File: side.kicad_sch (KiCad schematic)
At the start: 83 parts, among them J1 Conn_01x02, J2 SWD_Connector, J3 USB_C_Receptacle_USB2.0_14P, SW1 Reset Button, SW10 SW_Push, SW11 SW_Push, SW12 SW_Push, SW13 SW_Push, SW14 SW_Push, SW15 SW_Push, SW16 SW_Push, SW17 SW_Push, SW18 SW_Push, SW19 SW_Push, SW2 SW_On_Off, SW20 SW_Push, SW21 SW_Push, SW22 SW_Push, SW23 SW_Push, SW3 SW_Push, SW4 SW_Push, SW5 SW_Push, SW6 SW_Push, SW7 SW_Push, SW8 SW_Push, SW9 SW_Push, U1 nRF52840, U2 USBLC6-2SC6, Y1 JYJE 2TJ432000NYFBC

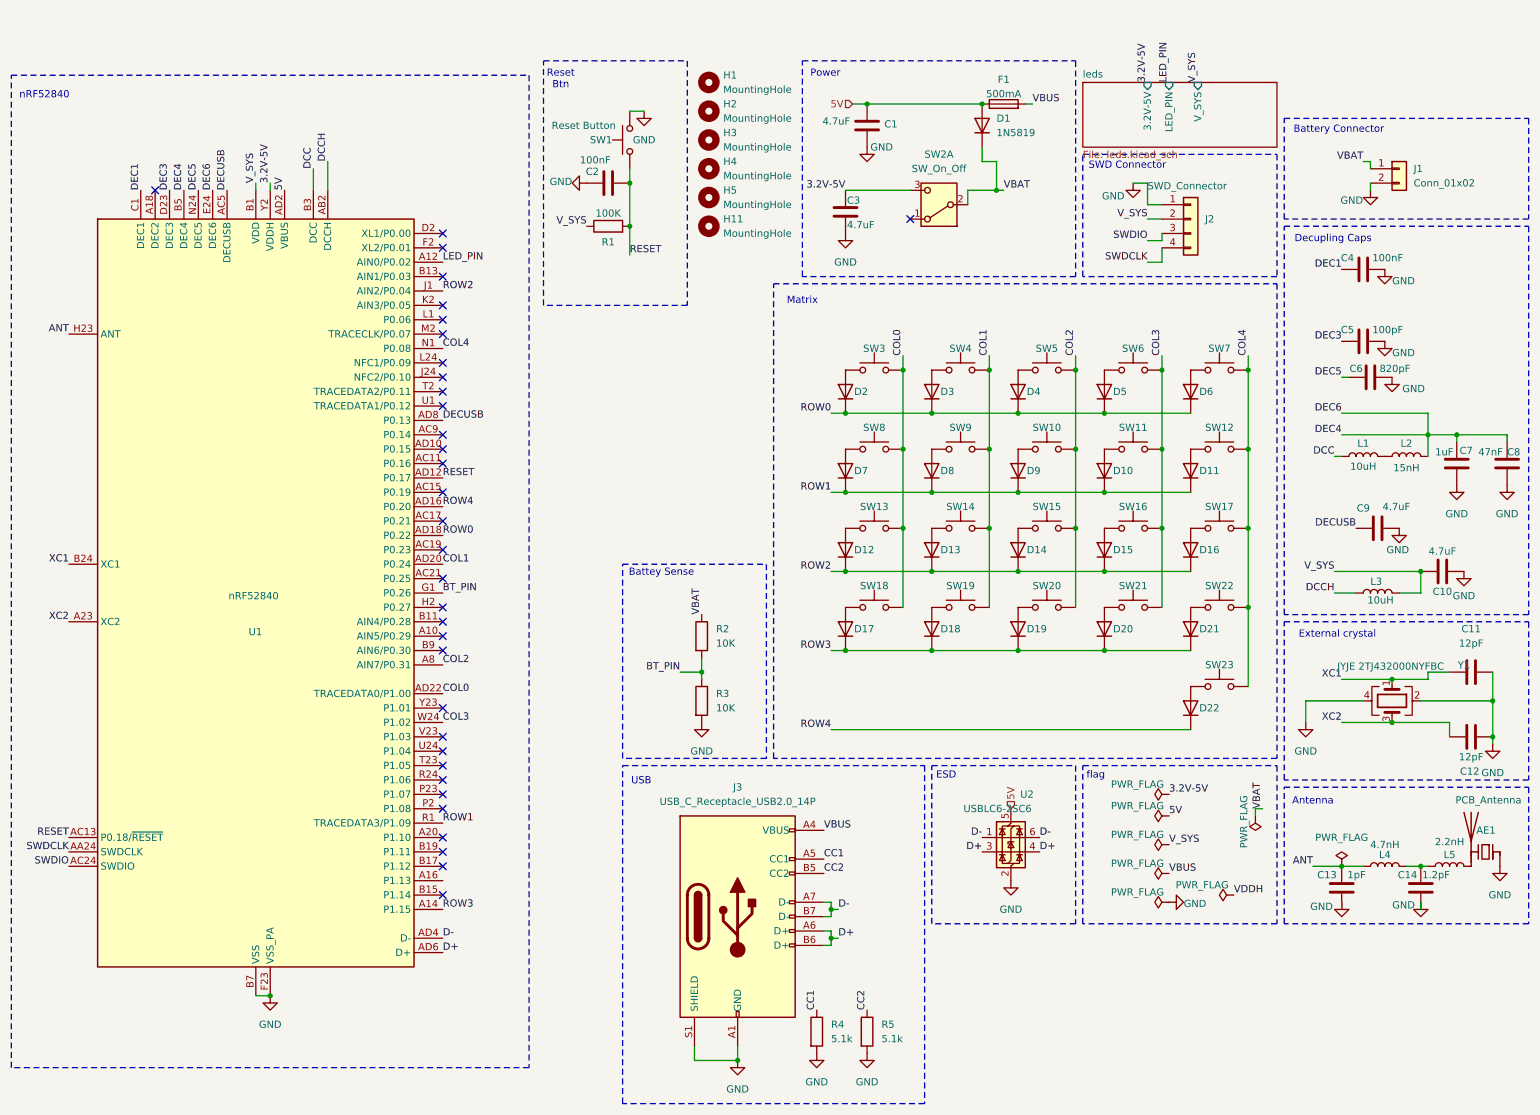
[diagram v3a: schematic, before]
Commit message: wired up the new votlage converter, removed small smd componenets
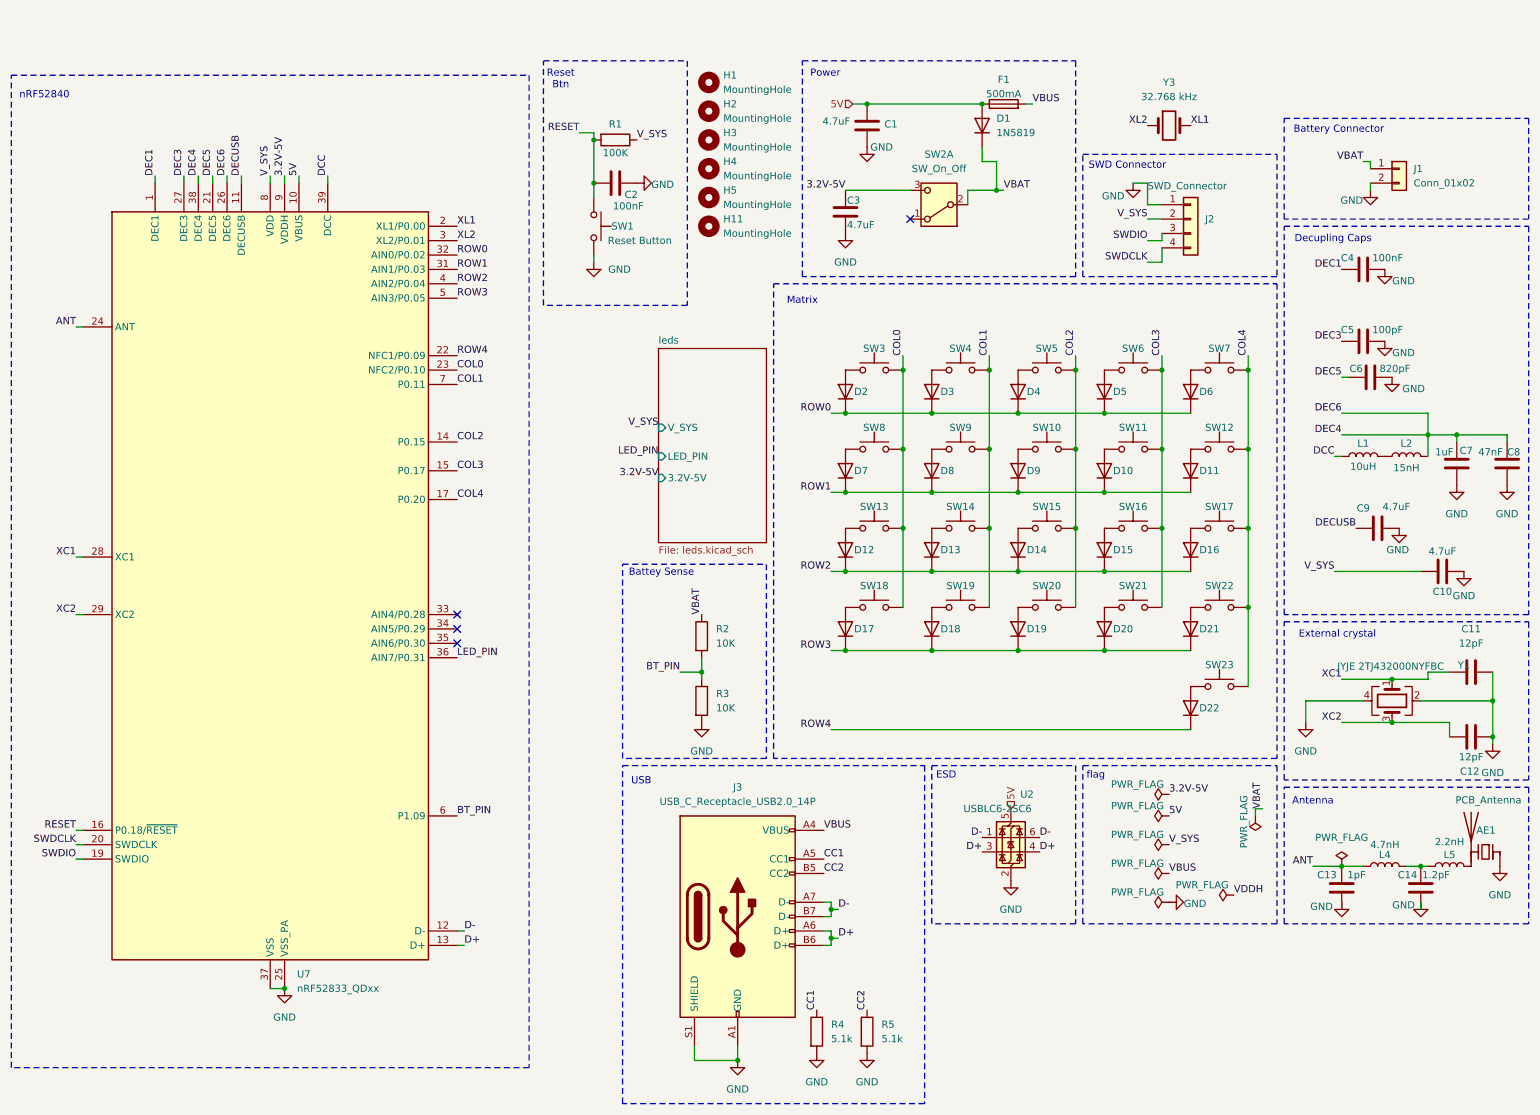
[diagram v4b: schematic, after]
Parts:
- removed L3: 10uH, Inductor_SMD:L_1008_2520Metric, symbol Device:L
- removed U1: nRF52840, Package_DFN_QFN:Nordic_AQFN-73-1EP_7x7mm_P0.5mm, symbol MCU_Nordic:nRF52840
- added U7: nRF52833_QDxx, Package_DFN_QFN:QFN-40-1EP_5x5mm_P0.4mm_EP3.6x3.6mm, symbol MCU_Nordic:nRF52833_QDxx
- added Y3: 32.768 kHz, Crystal:Crystal_SMD_3215-2Pin_3.2x1.5mm, symbol Device:Crystal
- C1, C10, C11, C12, C13, C14, C2, C3, C4, C5, C6, C7, C8, C9: footprint Capacitor_SMD:C_0402_1005Metric -> Capacitor_SMD:C_0603_1608Metric
- R1, R2, R3, R4, R5: footprint Resistor_SMD:R_0201_0603Metric -> Resistor_SMD:R_0402_1005Metric
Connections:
- net 3.2V-5V: now also U7.9 (VDDH)
- net 5V: now also U7.10 (VBUS)
- net ANT: now also U7.24 (ANT)
- net BT_PIN: now also U7.6 (P1.09)
- net COL0: now also U7.23 (NFC2/P0.10)
- net COL1: now also U7.7 (P0.11)
- net COL2: now also U7.14 (P0.15)
- net COL3: now also U7.15 (P0.17)
- net COL4: now also U7.17 (P0.20)
- net D+: now also U7.13 (D+)
- net D-: now also U7.12 (D-)
- net DCC: now also U7.39 (DCC)
- net DEC1: now also U7.1 (DEC1)
- net DEC3: now also U7.27 (DEC3)
- net DEC4: now also U7.26 (DEC6), U7.38 (DEC4)
- net DEC5: now also U7.21 (DEC5)
- net DECUSB: now also U7.11 (DECUSB)
- net GND: now also U7.25 (VSS_PA), U7.37 (VSS), U7.41 (VSS)
- net LED_PIN: now also U7.36 (AIN7/P0.31)
- net RESET: now also U7.16 (P0.18/~{RESET})
- net ROW0: now also U7.32 (AIN0/P0.02)
- net ROW1: now also U7.31 (AIN1/P0.03)
- net ROW2: now also U7.4 (AIN2/P0.04)
- net ROW3: now also U7.5 (AIN3/P0.05)
- net ROW4: now also U7.22 (NFC1/P0.09)
- net SWDCLK: now also U7.20 (SWDCLK)
- net SWDIO: now also U7.19 (SWDIO)
- net V_SYS: now also U7.18 (VDD), U7.30 (VDD), U7.40 (VDD), U7.8 (VDD)
- net XC1: now also U7.28 (XC1)
- net XC2: now also U7.29 (XC2)
- new net XL1: U7.2 (XL1/P0.00), Y3.2
- new net XL2: U7.3 (XL2/P0.01), Y3.1
- no-connect marks 34 -> 4
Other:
- moved on the sheet: C2, R1, SW1

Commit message: placed components
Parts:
- added C15, C31: 12pF, Capacitor_SMD:C_0402_1005Metric, symbol Device:C
- C10, C11, C12, C4, C5, C6, C7, C8, C9: footprint Capacitor_SMD:C_0603_1608Metric -> Capacitor_SMD:C_0402_1005Metric
- Y1: value JYJE 2TJ432000NYFBC -> 32MHz
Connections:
- net COL0: now also U7.34 (AIN5/P0.29); no longer U7.23 (NFC2/P0.10)
- net GND: now also C15.1, C31.1
- net LED_PIN: now also U7.33 (AIN4/P0.28); no longer U7.36 (AIN7/P0.31)
- net XL1: now also C31.2
- net XL2: now also C15.2
- net DEC4 renamed DEC4-6
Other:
- note added: "External crystal C"
- note added: "External crystal L"
- note added: "Mounting Holes"
- note removed: "External crystal"
- moved on the sheet: C2, C4, C6, H1, H11, H2, H3, H4, H5, J1, R1, SW1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

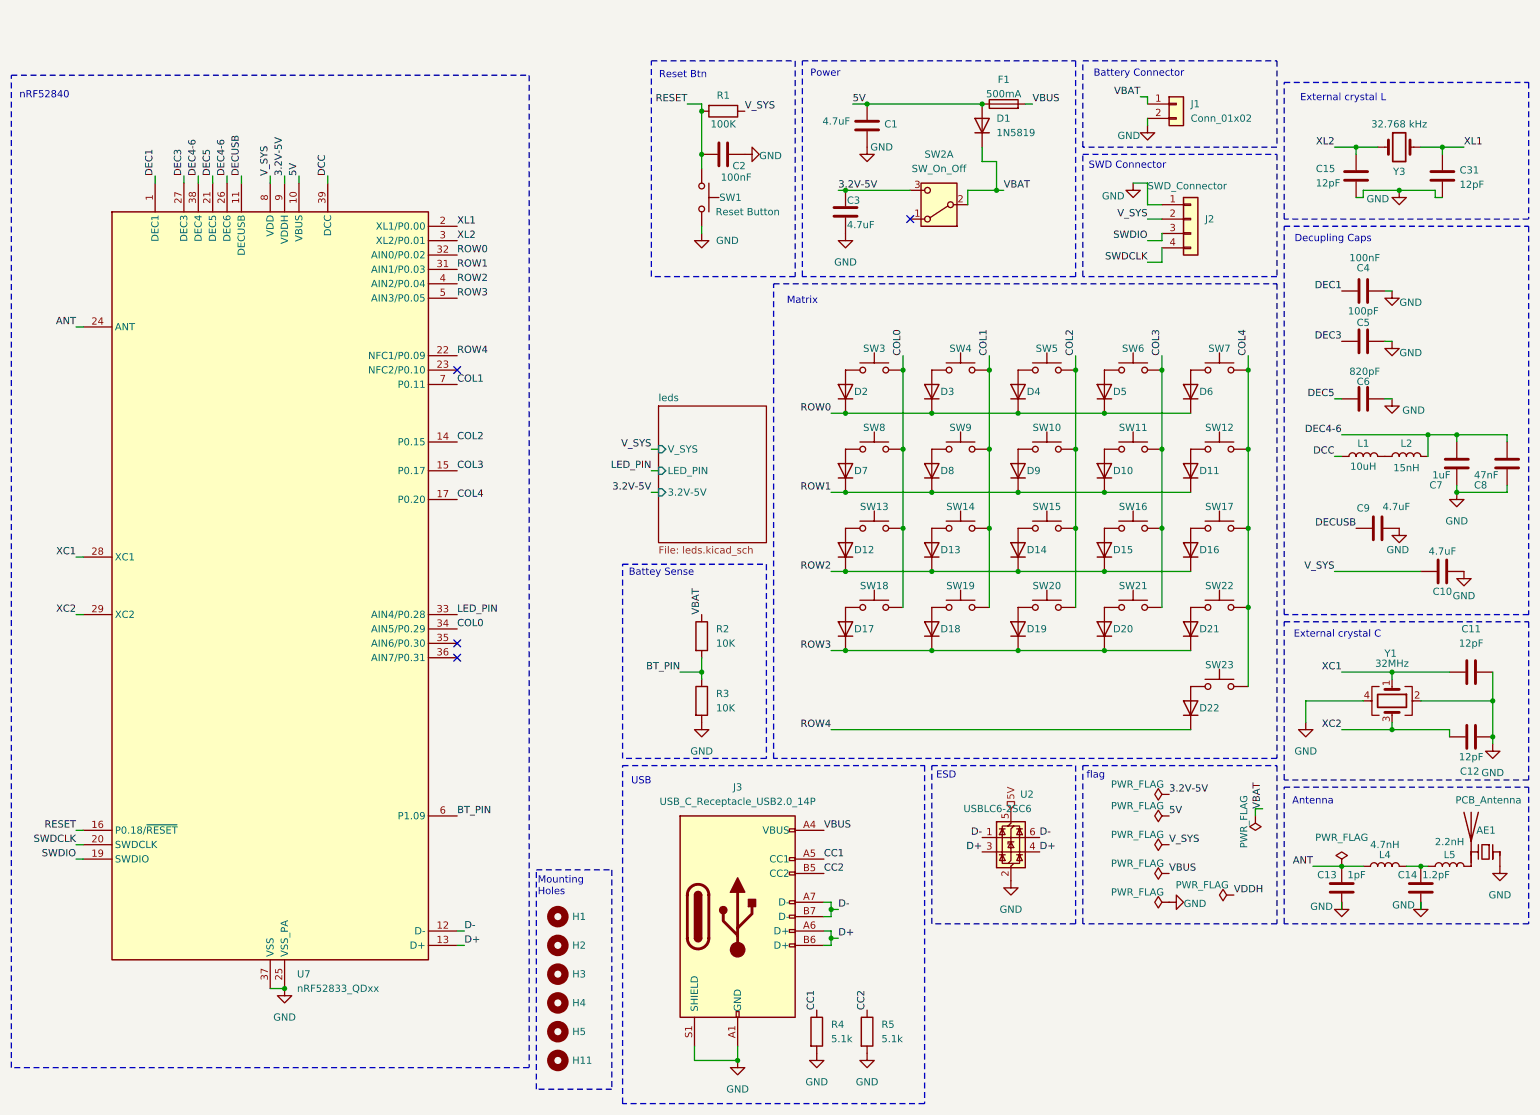
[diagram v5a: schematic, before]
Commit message: the right side still needs to be routed
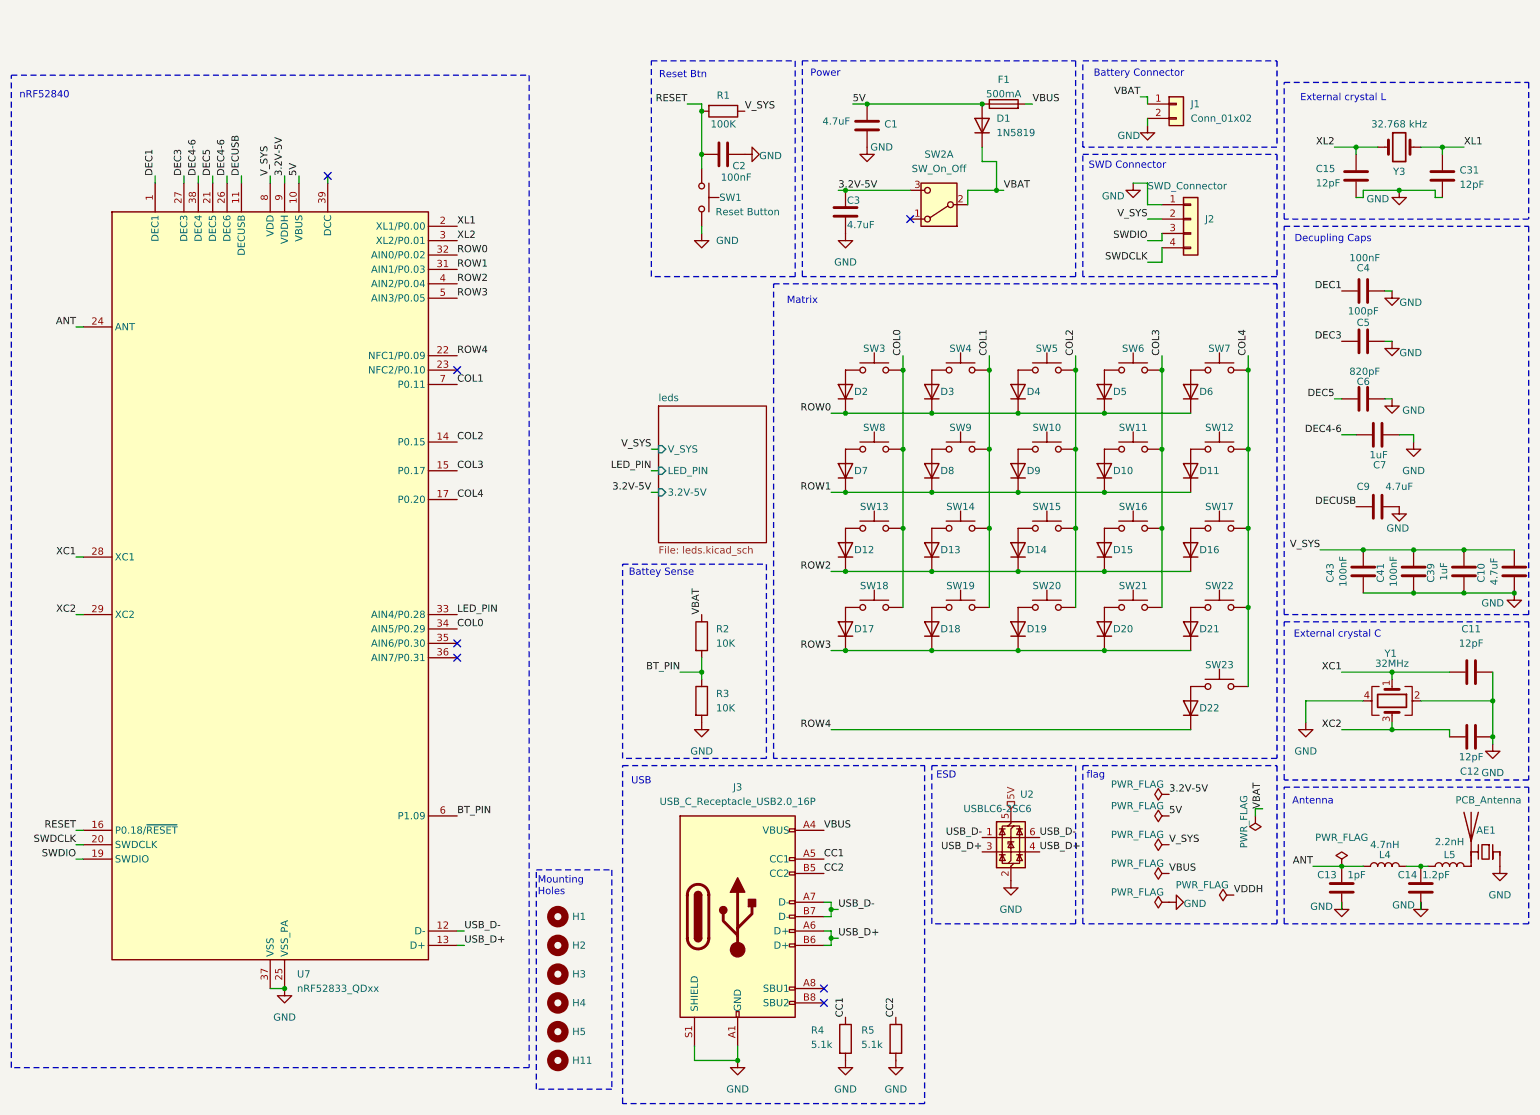
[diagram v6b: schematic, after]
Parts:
- removed C8: 47nF, Capacitor_SMD:C_0402_1005Metric, symbol Device:C
- removed J3: USB_C_Receptacle_USB2.0_14P, Connector_USB:USB_C_Receptacle_G-Switch_GT-USB-7025, symbol Connector:USB_C_Receptacle_USB2.0_14P
- removed L1: 10uH, Inductor_SMD:L_1008_2520Metric, symbol Device:L
- removed L2: 15nH, Inductor_SMD:L_0201_0603Metric, symbol Device:L
- added C39: 1uF, Capacitor_SMD:C_0402_1005Metric, symbol Device:C
- added C41, C43: 100nF, Capacitor_SMD:C_0402_1005Metric, symbol Device:C
- added J3: USB_C_Receptacle_USB2.0_16P, Connector_USB:USB_C_Receptacle_G-Switch_GT-USB-7025, symbol Connector:USB_C_Receptacle_USB2.0_16P
- C10: footprint Capacitor_SMD:C_0402_1005Metric -> Capacitor_SMD:C_0603_1608Metric
- L4, L5: footprint Inductor_SMD:L_0201_0603Metric -> Inductor_SMD:L_0402_1005Metric
- U7: LCSC (none) -> C2895249
- Y3: LCSC C5162538 -> C5213671
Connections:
- net CC1: now also J3.A5 (CC1)
- net CC2: now also J3.B5 (CC2)
- net GND: now also C10.1, C39.1, C41.1, C43.1, J3.A1 (GND), J3.A12 (GND), J3.B1 (GND), J3.B12 (GND), J3.S1 (SHIELD); no longer C10.2
- net VBUS: now also J3.A4 (VBUS), J3.A9 (VBUS), J3.B4 (VBUS), J3.B9 (VBUS)
- net V_SYS: now also C10.2, C39.2, C41.2, C43.2; no longer C10.1
- net D+ renamed USB_D+
- net USB_D+: now also J3.A6 (D+), J3.B6 (D+)
- net D- renamed USB_D-
- net USB_D-: now also J3.A7 (D-), J3.B7 (D-)
- net DCC: no longer names the net of U7.39 (DCC)
- no-connect marks 4 -> 7
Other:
- moved on the sheet: C10, C7, C9, R4, R5

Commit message: chaned usb c footprint, flipped fiducials
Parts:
- J3: footprint Connector_USB:USB_C_Receptacle_G-Switch_GT-USB-7025 -> Connector_USB:USB_C_Receptacle_G-Switch_GT-USB-7010ASV
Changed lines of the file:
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@@
 			)
 		)
-		(property "Footprint" "Connector_USB:USB_C_Receptacle_G-Switch_GT-USB-7025"
+		(property "Footprint" "Connector_USB:USB_C_Receptacle_G-Switch_GT-USB-7010ASV"
 			(at 146.05 163.83 0)
 			(effects
